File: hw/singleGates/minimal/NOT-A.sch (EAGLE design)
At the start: 3 parts, among them Q1 BC817

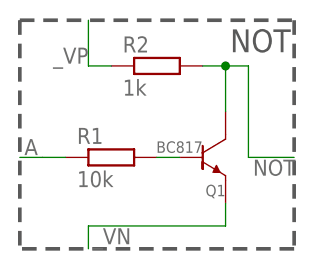
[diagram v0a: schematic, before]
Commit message: fixes alignment issues
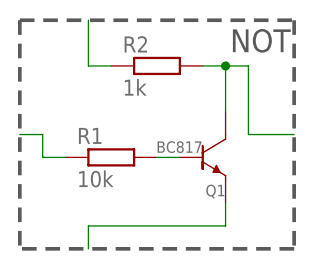
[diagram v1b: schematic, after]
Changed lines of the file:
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@@
 <wire x1="-2.54" y1="-10.16" x2="12.7" y2="-10.16" width="0.1524" layer="91"/>
 <wire x1="12.7" y1="-10.16" x2="12.7" y2="-7.62" width="0.1524" layer="91"/>
-<label x="-2.032" y="-12.192" size="1.778" layer="95"/>
 <wire x1="-2.54" y1="-10.16" x2="-2.54" y2="-12.7" width="0.1524" layer="91"/>
 <pinref part="Q1" gate="G$1" pin="EMITTER"/>
@@
 <wire x1="12.7" y1="2.54" x2="12.7" y2="7.62" width="0.1524" layer="91"/>
 <wire x1="12.7" y1="7.62" x2="15.24" y2="7.62" width="0.1524" layer="91"/>
-<wire x1="15.24" y1="7.62" x2="15.24" y2="-2.54" width="0.1524" layer="91"/>
-<wire x1="15.24" y1="-2.54" x2="20.32" y2="-2.54" width="0.1524" layer="91"/>
-<label x="15.748" y="-4.572" size="1.778" layer="95"/>
+<wire x1="15.24" y1="7.62" x2="15.24" y2="0" width="0.1524" layer="91"/>
+<wire x1="15.24" y1="0" x2="20.32" y2="0" width="0.1524" layer="91"/>
 <pinref part="R2" gate="G$1" pin="2"/>
 <wire x1="12.7" y1="7.62" x2="10.16" y2="7.62" width="0.1524" layer="91"/>
@@
 <pinref part="R1" gate="G$1" pin="1"/>
 <wire x1="-5.08" y1="-2.54" x2="-7.62" y2="-2.54" width="0.1524" layer="91"/>
-<wire x1="-7.62" y1="-2.54" x2="-10.16" y2="-2.54" width="0.1524" layer="91"/>
-<label x="-9.652" y="-2.286" size="1.778" layer="95"/>
+<wire x1="-7.62" y1="-2.54" x2="-7.62" y2="0" width="0.1524" layer="91"/>
+<wire x1="-7.62" y1="0" x2="-10.16" y2="0" width="0.1524" layer="91"/>
 </segment>
 </net>
@@
 <wire x1="0" y1="7.62" x2="-2.54" y2="7.62" width="0.1524" layer="91"/>
 <wire x1="-2.54" y1="7.62" x2="-2.54" y2="12.7" width="0.1524" layer="91"/>
-<label x="-2.54" y="9.652" size="1.778" layer="95" rot="R180"/>
 </segment>
 </net>

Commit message: Add led output and prepare first alu slice
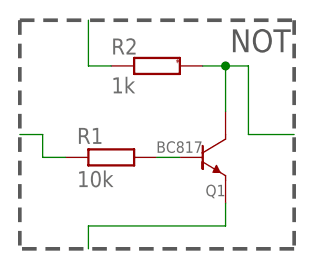
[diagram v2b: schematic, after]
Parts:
- R2: device p.peter-gator:R-EU_R0603 -> p.peter-rcl:R-EU-MARKEDR0603
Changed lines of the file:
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@@
 <parts>
 <part name="R1" library="p.peter-gator" deviceset="R-EU_" device="R0603" value="10k"/>
-<part name="R2" library="p.peter-gator" deviceset="R-EU_" device="R0603" value="1k"/>
+<part name="R2" library="p.peter-rcl" deviceset="R-EU-MARKED" device="R0603" value="1k"/>
 <part name="Q1" library="p.peter-gator" deviceset="TRANSISTOR-NPN-GENERIC" device="-SOT23-BEC" technology="DEFAULT" value="BC817"/>
 </parts>
